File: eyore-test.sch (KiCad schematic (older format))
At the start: 29 parts, among them P101 USB_5PIN_SHELL, P102 CONN_01X04, P103 CONN_01X02, SW101 SW_PUSHBUTTON, SW102 SW_PUSHBUTTON, U101 LD1117S33CTR, U102 STM32F072C8, U103 ESP-12E, U104 ESP-12E

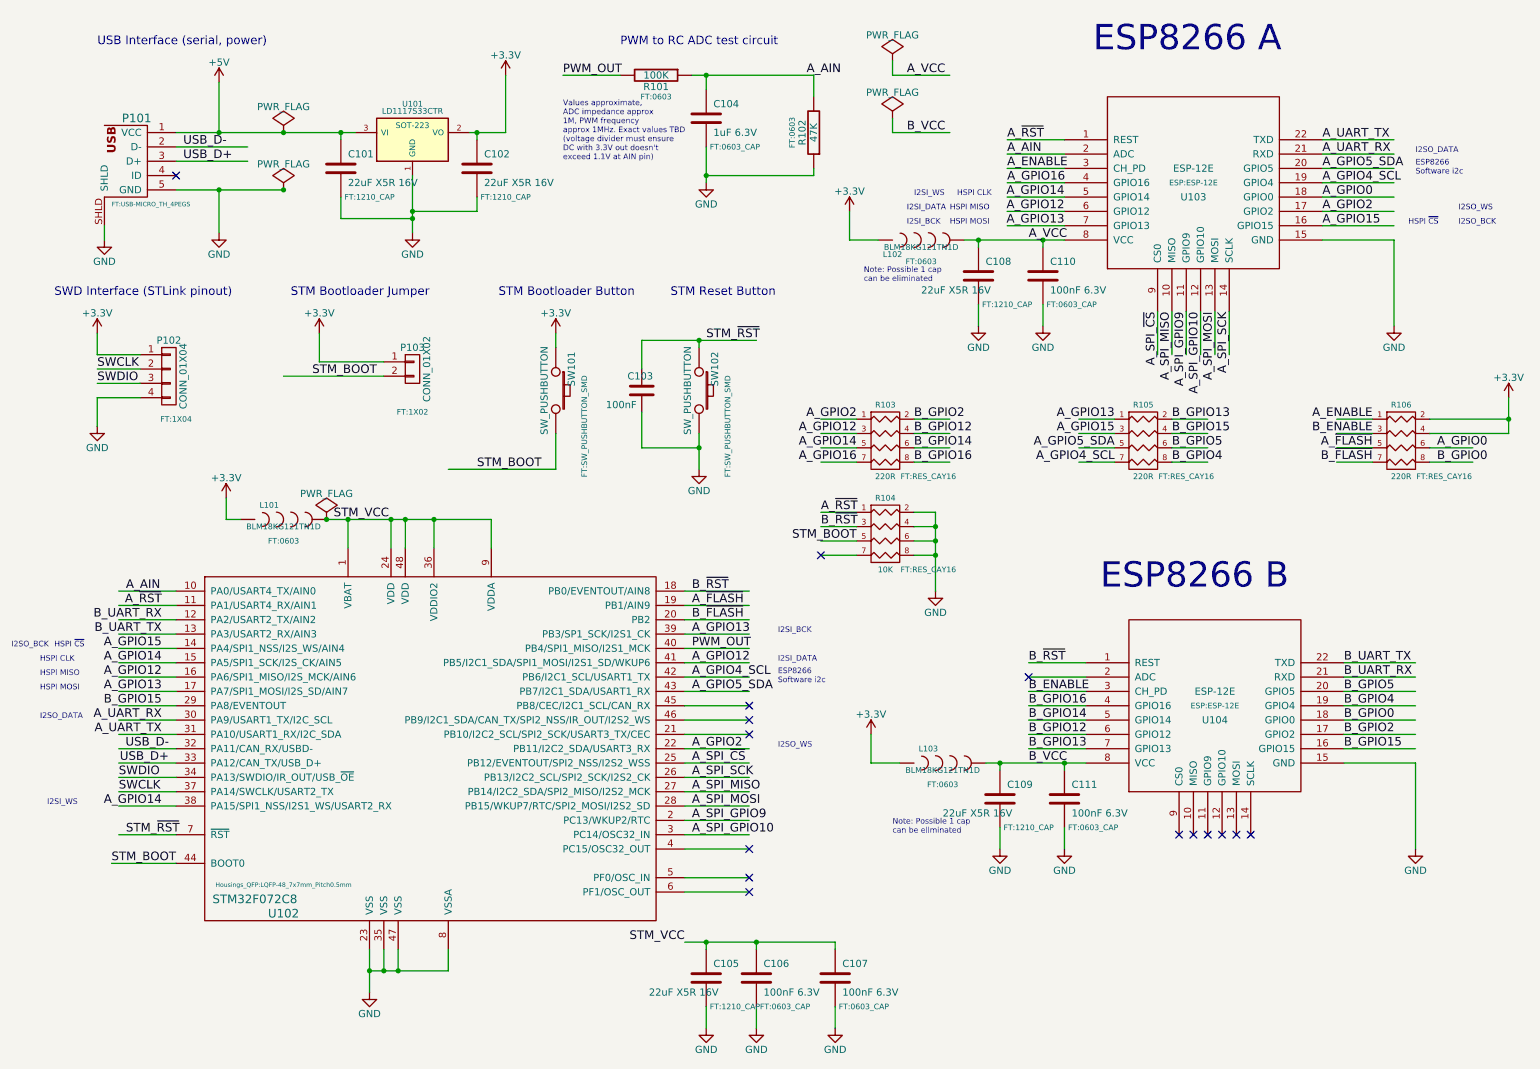
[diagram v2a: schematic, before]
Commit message: First cut at component layout
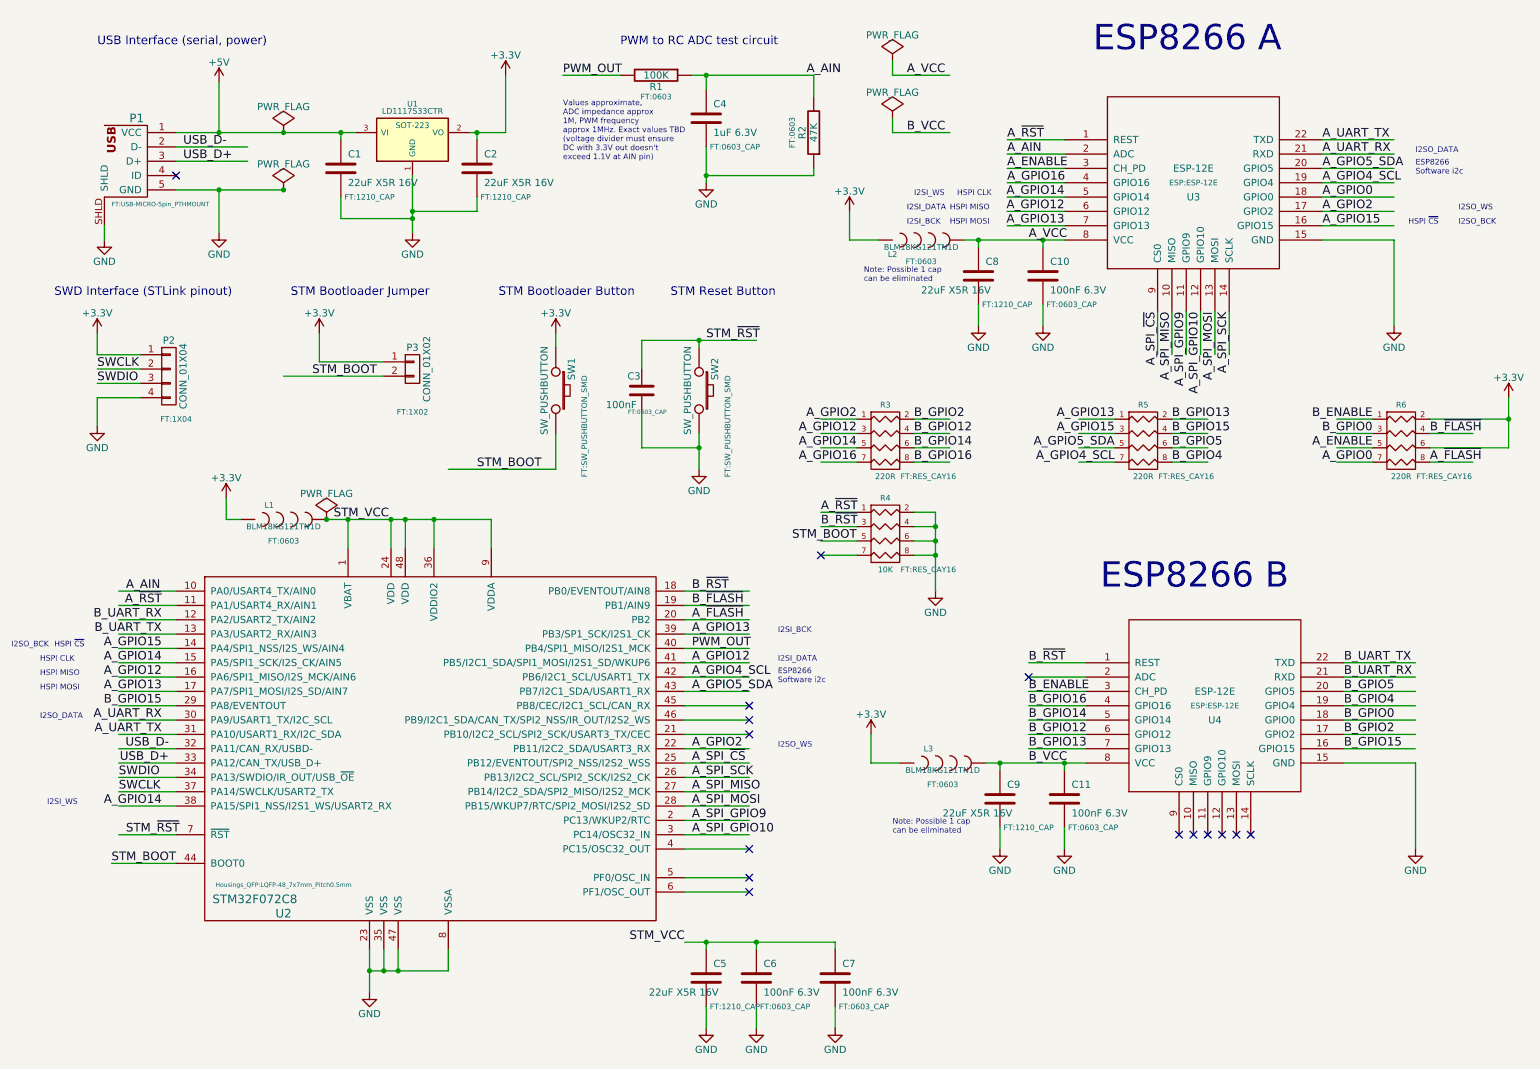
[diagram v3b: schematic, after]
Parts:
- C3: renamed from C103; footprint (none) -> FT:0603_CAP
- P1: renamed from P101; footprint FT:USB-MICRO_TH_4PEGS -> FT:USB-MICRO-5pin_PTHMOUNT
- renumbered C101 to C1, C110 to C10, C111 to C11, C102 to C2, C104 to C4, C105 to C5, C106 to C6, C107 to C7, C108 to C8, C109 to C9, L101 to L1, L102 to L2, L103 to L3, P102 to P2, P103 to P3, R101 to R1, R102 to R2, R103 to R3, R104 to R4, R105 to R5, R106 to R6, SW101 to SW1, SW102 to SW2, U101 to U1, U102 to U2, U103 to U3, U104 to U4
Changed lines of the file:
@@
 $EndDescr
 $Comp
-L USB_5PIN_SHELL P101
+L USB_5PIN_SHELL P1
 U 1 1 56305F6A
 P 1450 1450
-F 0 "P101" H 1375 1700 60  0000 C CNN
+F 0 "P1" H 1375 1700 60  0000 C CNN
 F 1 "USB_5PIN_SHELL" H 1300 1100 60  0001 L CNN
-F 2 "FT:USB-MICRO_TH_4PEGS" H 1200 1100 31  0000 L CNN
+F 2 "FT:USB-MICRO-5pin_PTHMOUNT" H 1200 1100 31  0000 L CNN
 F 3 "" H 1450 1450 60  0000 C CNN
 	1    1450 1450
@@
 $EndComp
 $Comp
-L LD1117S33CTR U101
+L LD1117S33CTR U1
 U 1 1 56306091
 P 3300 1350
-F 0 "U101" H 3300 1600 40  0000 C CNN
+F 0 "U1" H 3300 1600 40  0000 C CNN
 F 1 "LD1117S33CTR" H 3300 1550 40  0000 C CNN
 F 2 "SOT-223" H 3300 1450 40  0000 C CNN
@@
 NoConn ~ 1650 1600
 $Comp
-L CONN_01X04 P102
+L CONN_01X04 P2
 U 1 1 56306A52
 P 1600 3000
-F 0 "P102" H 1600 3250 50  0000 C CNN
+F 0 "P2" H 1600 3250 50  0000 C CNN
 F 1 "CONN_01X04" V 1700 3000 50  0000 C CNN
 F 2 "FT:1X04" H 1650 2700 39  0000 C CNN
@@
 ESP8266 B
 $Comp
-L CAP C101
+L CAP C1
 U 1 1 563169F8
 P 2800 1550
-F 0 "C101" H 2850 1650 50  0000 L CNN
+F 0 "C1" H 2850 1650 50  0000 L CNN
 F 1 "22uF X5R 16V" H 2850 1450 50  0000 L CNN
 F 2 "FT:1210_CAP" H 3000 1350 39  0000 C CNN
@@
 $EndComp
 $Comp
-L CAP C102
+L CAP C2
 U 1 1 563168AB
 P 3750 1550
-F 0 "C102" H 3800 1650 50  0000 L CNN
+F 0 "C2" H 3800 1650 50  0000 L CNN
 F 1 "22uF X5R 16V" H 3800 1450 50  0000 L CNN
 F 2 "FT:1210_CAP" H 3950 1350 39  0000 C CNN
@@
 $EndComp
 $Comp
-L ESP-12E U103
+L ESP-12E U3
 U 1 1 5631671A
 P 8750 1650
-F 0 "U103" H 8750 1550 50  0000 C CNN
+F 0 "U3" H 8750 1550 50  0000 C CNN
 F 1 "ESP-12E" H 8750 1750 50  0000 C CNN
 F 2 "ESP:ESP-12E" H 8750 1650 39  0000 C CNN
@@
 $EndComp
 $Comp
-L CAP C110
+L CAP C10
 U 1 1 56317877
 P 7700 2300
-F 0 "C110" H 7750 2400 50  0000 L CNN
+F 0 "C10" H 7750 2400 50  0000 L CNN
 F 1 "100nF 6.3V" H 7750 2200 50  0000 L CNN
 F 2 "FT:0603_CAP" H 7900 2100 39  0000 C CNN
@@
 $EndComp
 $Comp
-L CAP C108
+L CAP C8
 U 1 1 56317F18
 P 7250 2300
-F 0 "C108" H 7300 2400 50  0000 L CNN
+F 0 "C8" H 7300 2400 50  0000 L CNN
 F 1 "22uF X5R 16V" H 6850 2200 50  0000 L CNN
 F 2 "FT:1210_CAP" H 7450 2100 39  0000 C CNN
@@
 Note: Possible 1 cap\ncan be eliminated
 $Comp
-L ESP-12E U104
+L ESP-12E U4
 U 1 1 56319075
 P 8900 5300
-F 0 "U104" H 8900 5200 50  0000 C CNN
+F 0 "U4" H 8900 5200 50  0000 C CNN
 F 1 "ESP-12E" H 8900 5400 50  0000 C CNN
 F 2 "ESP:ESP-12E" H 8900 5300 39  0000 C CNN
@@
 $EndComp
 $Comp
-L CAP C111
+L CAP C11
 U 1 1 563190A8
 P 7850 5950
-F 0 "C111" H 7900 6050 50  0000 L CNN
+F 0 "C11" H 7900 6050 50  0000 L CNN
 F 1 "100nF 6.3V" H 7900 5850 50  0000 L CNN
 F 2 "FT:0603_CAP" H 8050 5750 39  0000 C CNN
@@
 $EndComp
 $Comp
-L CAP C109
+L CAP C9
 U 1 1 563190BB
 P 7400 5950
-F 0 "C109" H 7450 6050 50  0000 L CNN
+F 0 "C9" H 7450 6050 50  0000 L CNN
 F 1 "22uF X5R 16V" H 7000 5850 50  0000 L CNN
 F 2 "FT:1210_CAP" H 7600 5750 39  0000 C CNN
@@
 NoConn ~ 9150 6200
 $Comp
-L R_PACK4 R103
+L R_PACK4 R3
 U 1 1 56319BA9
 P 6600 3650
-F 0 "R103" H 6600 4100 40  0000 C CNN
+F 0 "R3" H 6600 4100 40  0000 C CNN
 F 1 "220R" H 6600 3600 40  0000 C CNN
 F 2 "FT:RES_CAY16" H 6900 3600 39  0000 C CNN
@@
 Text Label 5250 4500 0    60   ~ 0
 B_~RST
-Text Label 5250 4600 0    60   ~ 0
+Text Label 5250 4700 0    60   ~ 0
 A_~FLASH
 Text Label 1550 5500 2    60   ~ 0
@@
 Text Label 6400 3500 2    60   ~ 0
 A_GPIO14
-Text Label 10450 3500 0    60   ~ 0
+Text Label 10000 3600 2    60   ~ 0
 A_GPIO0
 Text Label 6800 3400 0    60   ~ 0
@@
 STM Bootloader Jumper\n
 $Comp
-L R R101
+L R R1
 U 1 1 5631CB53
 P 5000 900
-F 0 "R101" V 5080 900 50  0000 C CNN
+F 0 "R1" V 5080 900 50  0000 C CNN
 F 1 "100K" V 5000 900 50  0000 C CNN
 F 2 "FT:0603" V 5150 900 39  0000 C CNN
@@
 $EndComp
 $Comp
-L CAP C104
+L CAP C4
 U 1 1 5631CC77
 P 5350 1200
-F 0 "C104" H 5400 1300 50  0000 L CNN
+F 0 "C4" H 5400 1300 50  0000 L CNN
 F 1 "1uF 6.3V" H 5400 1100 50  0000 L CNN
 F 2 "FT:0603_CAP" H 5550 1000 39  0000 C CNN
@@
 Values approximate,\nADC impedance approx\n1M, PWM frequency\napprox 1MHz. Exact values TBD\n(voltage divider must ensure\nDC with 3.3V out doesn't\nexceed 1.1V at AIN pin)
 $Comp
-L R R102
+L R R2
 U 1 1 5631E0A5
 P 6100 1300
-F 0 "R102" V 6180 1300 50  0000 C CNN
+F 0 "R2" V 6180 1300 50  0000 C CNN
 F 1 "47K" V 6100 1300 50  0000 C CNN
 F 2 "FT:0603" V 6250 1300 39  0000 C CNN
@@
 $EndComp
 $Comp
-L INDUCTOR L101
+L INDUCTOR L1
 U 1 1 5632781C
 P 2400 4000
-F 0 "L101" H 2300 4100 40  0000 C CNN
+F 0 "L1" H 2300 4100 40  0000 C CNN
 F 1 "BLM18KG121TN1D" H 2400 3950 40  0000 C CNN
 F 2 "FT:0603" H 2400 3850 39  0000 C CNN
@@
 STM_VCC
 $Comp
-L CAP C106
+L CAP C6
 U 1 1 5632809E
 P 5700 7200
-F 0 "C106" H 5750 7300 50  0000 L CNN
+F 0 "C6" H 5750 7300 50  0000 L CNN
 F 1 "100nF 6.3V" H 5750 7100 50  0000 L CNN
 F 2 "FT:0603_CAP" H 5900 7000 39  0000 C CNN
@@
 $EndComp
 $Comp
-L CAP C105
+L CAP C5
 U 1 1 563280AB
 P 5350 7200
-F 0 "C105" H 5400 7300 50  0000 L CNN
+F 0 "C5" H 5400 7300 50  0000 L CNN
 F 1 "22uF X5R 16V" H 4950 7100 50  0000 L CNN
 F 2 "FT:1210_CAP" H 5550 7000 39  0000 C CNN
@@
 NoConn ~ 5650 6600
 $Comp
-L CONN_01X02 P103
+L CONN_01X02 P3
 U 1 1 56329079
 P 3300 2950
-F 0 "P103" H 3300 3100 50  0000 C CNN
+F 0 "P3" H 3300 3100 50  0000 C CNN
 F 1 "CONN_01X02" V 3400 2950 50  0000 C CNN
 F 2 "FT:1X02" H 3300 2650 39  0000 C CNN
@@
 $EndComp
 $Comp
-L SW_PUSHBUTTON SW101
+L SW_PUSHBUTTON SW1
 U 1 1 5632913A
 P 4300 3100
-F 0 "SW101" H 4150 3210 50  0000 C CNN
+F 0 "SW1" H 4150 3210 50  0000 C CNN
 F 1 "SW_PUSHBUTTON" H 4300 3020 50  0000 C CNN
 F 2 "FT:SW_PUSHBUTTON_SMD" H 4550 3300 39  0000 C CNN
@@
 PWM_OUT
 $Comp
-L SW_PUSHBUTTON SW102
+L SW_PUSHBUTTON SW2
 U 1 1 5633117C
 P 5300 3100
-F 0 "SW102" H 5150 3210 50  0000 C CNN
+F 0 "SW2" H 5150 3210 50  0000 C CNN
 F 1 "SW_PUSHBUTTON" H 5300 3020 50  0000 C CNN
 F 2 "FT:SW_PUSHBUTTON_SMD" H 5550 3300 39  0000 C CNN
@@
 $EndComp
 $Comp
-L INDUCTOR L102
+L INDUCTOR L2
 U 1 1 56331B2E
 P 6850 2050
-F 0 "L102" H 6650 1950 40  0000 C CNN
+F 0 "L2" H 6650 1950 40  0000 C CNN
 F 1 "BLM18KG121TN1D" H 6850 2000 40  0000 C CNN
 F 2 "FT:0603" H 6850 1900 39  0000 C CNN
@@
 $EndComp
 $Comp
-L INDUCTOR L103
+L INDUCTOR L3
 U 1 1 56331D88
 P 7000 5700
-F 0 "L103" H 6900 5800 40  0000 C CNN
+F 0 "L3" H 6900 5800 40  0000 C CNN
 F 1 "BLM18KG121TN1D" H 7000 5650 40  0000 C CNN
 F 2 "FT:0603" H 7000 5550 39  0000 C CNN
@@
 $EndComp
 $Comp
-L R_PACK4 R105
+L R_PACK4 R5
 U 1 1 563332AA
 P 8400 3650
-F 0 "R105" H 8400 4100 40  0000 C CNN
+F 0 "R5" H 8400 4100 40  0000 C CNN
 F 1 "220R" H 8400 3600 40  0000 C CNN
 F 2 "FT:RES_CAY16" H 8700 3600 39  0000 C CNN
@@
 $EndComp
 $Comp
-L R_PACK4 R106
+L R_PACK4 R6
 U 1 1 5633332C
 P 10200 3650
-F 0 "R106" H 10200 4100 40  0000 C CNN
+F 0 "R6" H 10200 4100 40  0000 C CNN
 F 1 "220R" H 10200 3600 40  0000 C CNN
 F 2 "FT:RES_CAY16" H 10500 3600 39  0000 C CNN
@@
 	1    0    0    -1
 $EndComp
-Text Label 10000 3400 2    60   ~ 0
+Text Label 10000 3300 2    60   ~ 0
 B_ENABLE
-Text Label 10000 3300 2    60   ~ 0
+Text Label 10000 3500 2    60   ~ 0
 A_ENABLE
 Text Label 1550 5300 2    60   ~ 0
@@
 	7600 5200 8000 5200
 Wire Wire Line
-	10950 3400 10400 3400
-Wire Wire Line
 	10000 3500 9750 3500
 Wire Wire Line
@@
 Wire Wire Line
 	10000 3300 9750 3300
-Wire Wire Line
-	10400 3300 10950 3300
 Connection ~ 3250 4000
 Wire Wire Line
@@
 	5200 4700 5650 4700
 $Comp
-L CAP C107
+L CAP C7
 U 1 1 5642561E
 P 6250 7200
-F 0 "C107" H 6300 7300 50  0000 L CNN
+F 0 "C7" H 6300 7300 50  0000 L CNN
 F 1 "100nF 6.3V" H 6300 7100 50  0000 L CNN
 F 2 "FT:0603_CAP" H 6450 7000 39  0000 C CNN
@@
 I2SI_WS
 $Comp
-L STM32F072C8 U102
+L STM32F072C8 U2
 U 1 1 56430488
 P 3300 5500
-F 0 "U102" H 2400 4250 60  0000 C CNN
+F 0 "U2" H 2400 4250 60  0000 C CNN
 F 1 "STM32F072C8" H 2200 4350 60  0000 C CNN
 F 2 "Housings_QFP:LQFP-48_7x7mm_Pitch0.5mm" H 2400 4450 31  0000 C CNN
@@
 B_~RST
 $Comp
-L R_PACK4 R104
+L R_PACK4 R4
 U 1 1 564388E3
 P 6600 4300
-F 0 "R104" H 6600 4750 40  0000 C CNN
+F 0 "R4" H 6600 4750 40  0000 C CNN
 F 1 "10K" H 6600 4250 40  0000 C CNN
 F 2 "FT:RES_CAY16" H 6900 4250 39  0000 C CNN
@@
 	5200 6950 6250 6950
 $Comp
-L C C103
+L C C3
 U 1 1 56447F1C
 P 4900 3100
-F 0 "C103" H 4800 3200 50  0000 L CNN
+F 0 "C3" H 4800 3200 50  0000 L CNN
 F 1 "100nF" H 4650 3000 50  0000 L CNN
-F 2 "" H 4938 2950 30  0000 C CNN
+F 2 "FT:0603_CAP" H 4938 2950 30  0000 C CNN
 F 3 "" H 4900 3100 60  0000 C CNN
 	1    4900 3100
@@
 	4900 3500 4900 3250
 Connection ~ 5300 3500
-Text Label 5250 4700 0    60   ~ 0
+Text Label 5250 4600 0    60   ~ 0
 B_~FLASH
-Text Label 10000 3500 2    60   ~ 0
+Text Label 10400 3600 0    60   ~ 0
 A_~FLASH
 Wire Wire Line
-	10950 3150 10950 3400
+	10950 3500 10950 3150
 Connection ~ 10950 3300
-Text Label 10000 3600 2    60   ~ 0
+Text Label 10400 3400 0    60   ~ 0
 B_~FLASH
 Wire Wire Line
 	10000 3600 9750 3600
 Wire Wire Line
-	10400 3500 10700 3500
-Text Label 10450 3600 0    60   ~ 0
+	10400 3500 10950 3500
+Text Label 10000 3400 2    60   ~ 0
 B_GPIO0
 Wire Wire Line
 	10400 3600 10700 3600
+Wire Wire Line
+	10400 3300 10950 3300
+Wire Wire Line
+	10400 3400 10700 3400
 $EndSCHEMATC
